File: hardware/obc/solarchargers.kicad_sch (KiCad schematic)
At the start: 36 parts, among them U105 LTC4121, U402 LTC4121

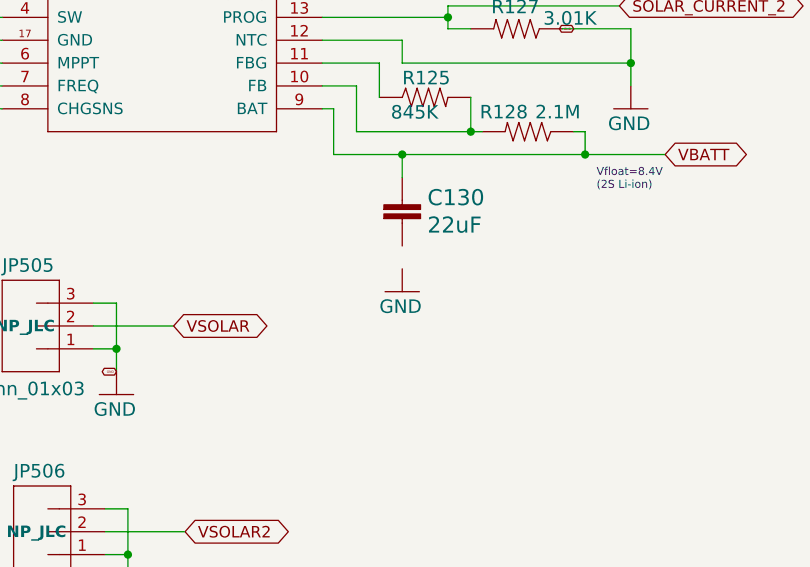
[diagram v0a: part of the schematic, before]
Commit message: OBC: Continuing work towards the next revision
- tidied up Radio and GPS page
- moved J305 to Avionics page
- changed R423 to 1.5k
- removed R428 so ILIM pin connects directly to GNDREF
- changed L403 to 4.7uH
- deleted BOM fields proto and flight
- connected C130 to ground
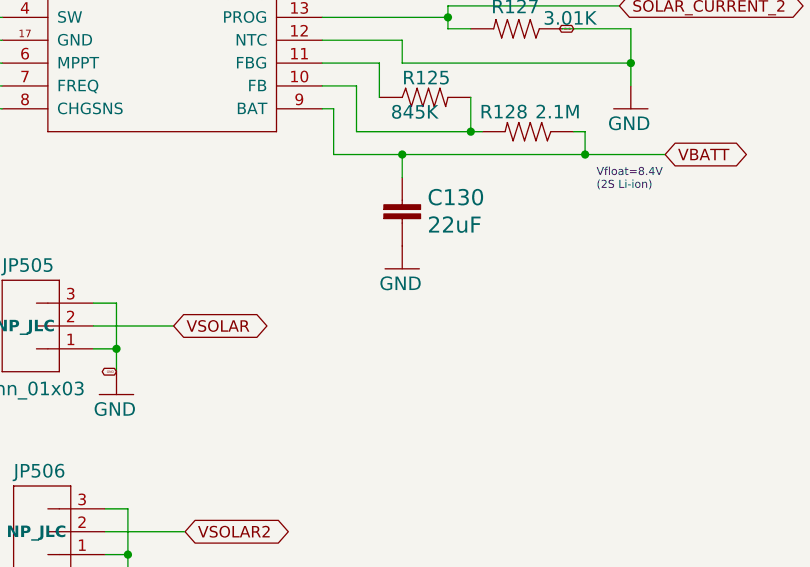
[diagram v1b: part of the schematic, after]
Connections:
- net GND: now also C130.2
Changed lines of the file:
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@@
 	(symbol
 		(lib_id "mainboard:GND")
-		(at 146.05 153.67 0)
+		(at 146.05 151.13 0)
 		(unit 1)
 		(exclude_from_sim no)
@@
 		(dnp no)
 		(property "Reference" "#GND0124"
-			(at 146.05 153.67 0)
+			(at 146.05 151.13 0)
 			(effects
 				(font
@@
 		)
 		(property "Value" "GND"
-			(at 143.51 156.21 0)
+			(at 143.51 153.67 0)
 			(effects
 				(font
@@
 		)
 		(property "Footprint" ""
-			(at 146.05 153.67 0)
+			(at 146.05 151.13 0)
 			(effects
 				(font
@@
 		)
 		(property "Datasheet" ""
-			(at 146.05 153.67 0)
+			(at 146.05 151.13 0)
 			(effects
 				(font
@@
 		)
 		(property "Description" ""
-			(at 146.05 153.67 0)
+			(at 146.05 151.13 0)
 			(effects
 				(font

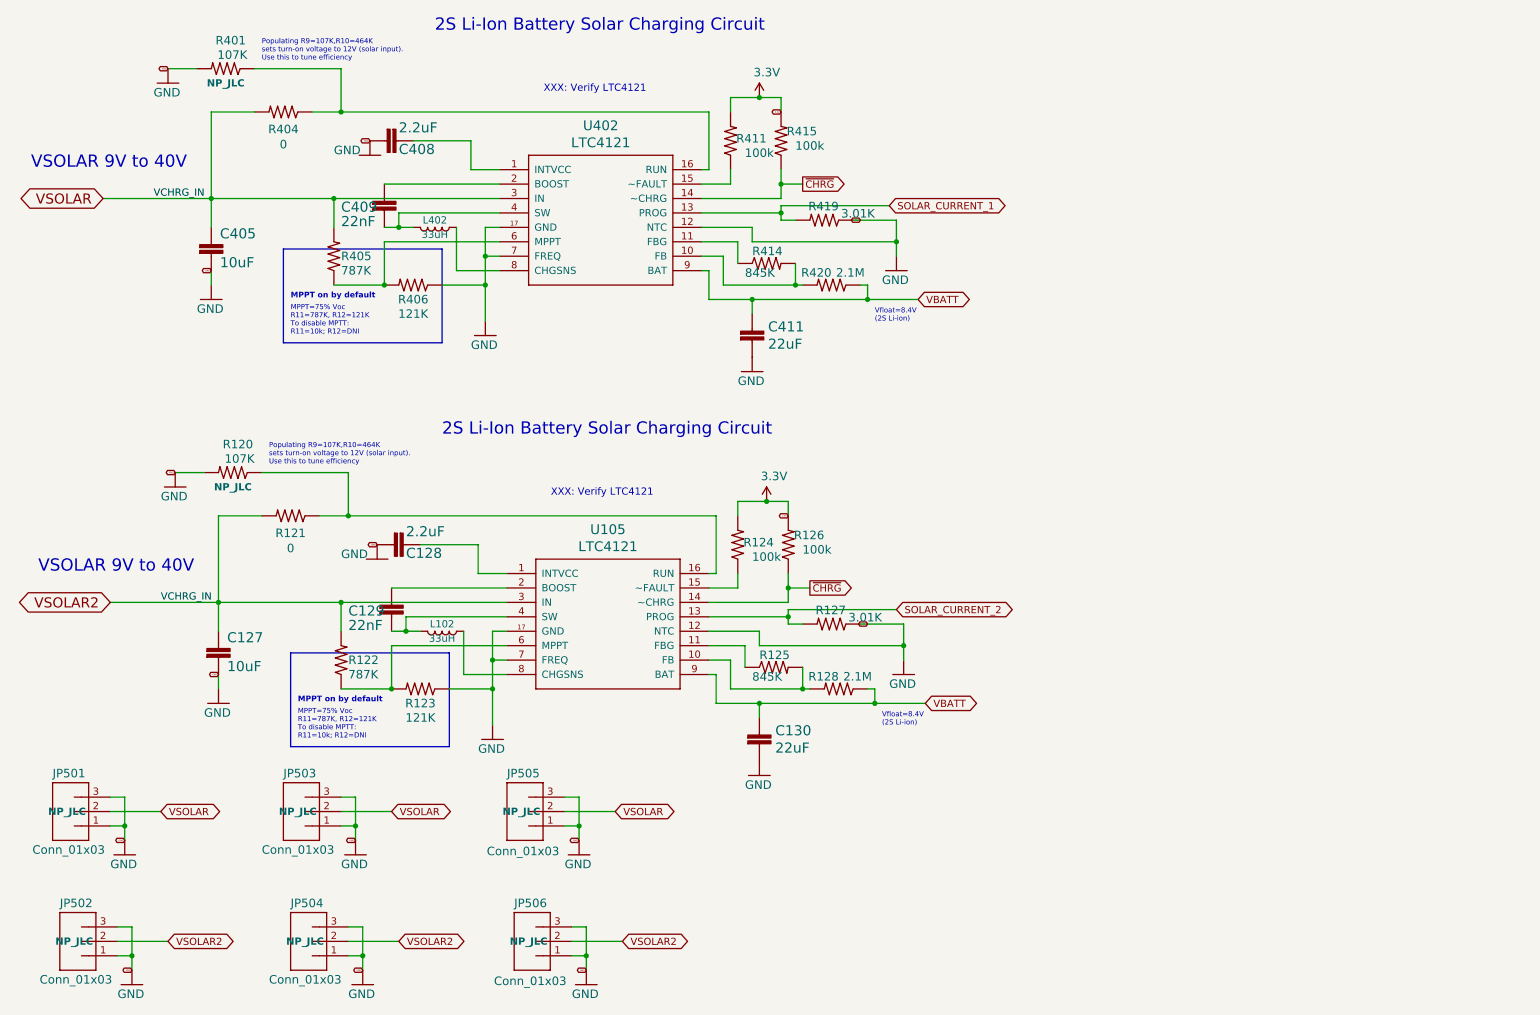
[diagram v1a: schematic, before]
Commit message: OBC: Continuing work towards the next revision
- moved Jtag to Avionics page
- re-aligned and removed excess text
- flipped watchdog to make +3.3v face up
- cleaned up VREG pins, crystal, SWCLK, SWDIO, and watch dog connections
- fixed MRAM symbol
- changed USB_D +/- resistor values
- spaced out schematics on power and burn wire pages
- fixed GNDREF connection for J302
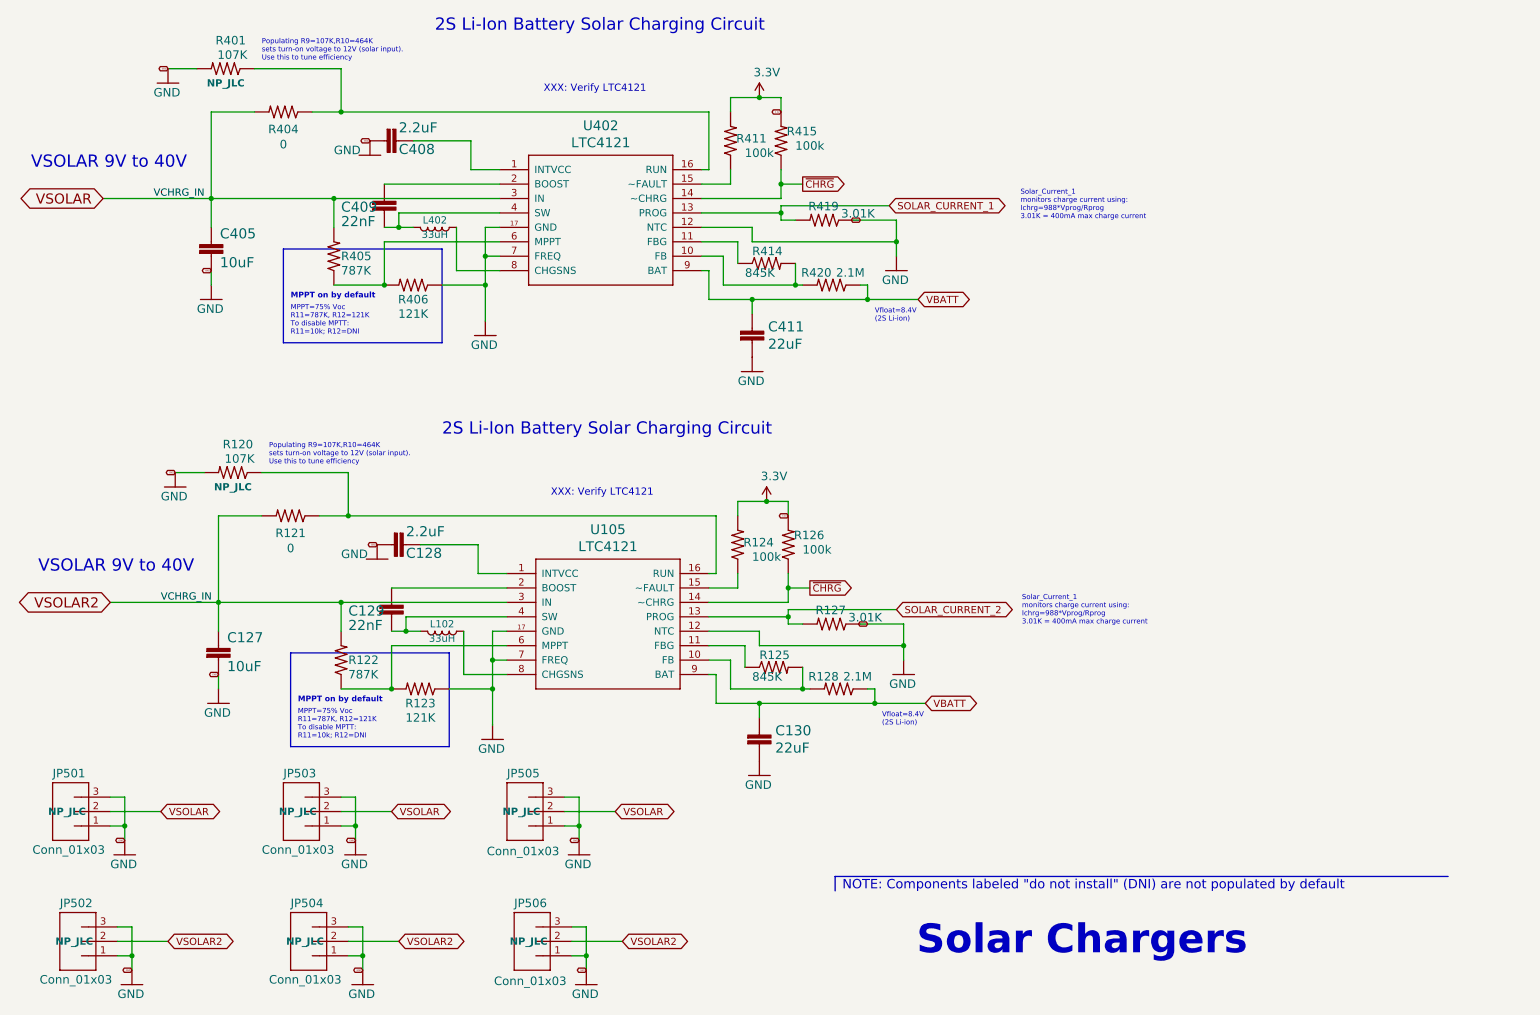
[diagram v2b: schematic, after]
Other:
- note added: "NOTE: Components labeled "do not install" (DNI) are not populated by default"
- note added: "Solar Chargers"
- note added: "Solar_Current_1 monitors charge current using: Ichrg=988*Vprog/Rprog 3.01K = 400mA max charge current"
- title: (none) -> Obi Wan Computer
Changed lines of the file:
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@@
 	(generator "eeschema")
 	(generator_version "8.0")
-	(paper "A4")
+	(paper "USLetter")
+	(title_block
+		(title "Obi Wan Computer")
+		(rev "1")
+	)
 	(junction
 		(at 166.37 138.43)
@@
 		)
 	)
+	(polyline
+		(pts
+			(xy 159.385 171.45) (xy 159.385 168.91)
+		)
+		(stroke
+			(width 0)
+			(type default)
+		)
+	)
 	(wire
 		(pts
@@
 		(pts
 			(xy 49.53 34.29) (xy 49.53 49.53)
+		)
+		(stroke
+			(width 0)
+			(type default)
+		)
+	)
+	(polyline
+		(pts
+			(xy 159.385 168.91) (xy 267.335 168.91)
 		)
 		(stroke
@@
 			(font
 				(size 0.889 0.889)
+			)
+			(justify left bottom)
+		)
+	)
+	(text "NOTE: Components labeled \"do not install\" (DNI) are not populated by default"
+		(exclude_from_sim no)
+		(at 160.655 171.45 0)
+		(effects
+			(font
+				(size 1.651 1.651)
 			)
 			(justify left bottom)
@@
 		)
 	)
+	(text "Solar Chargers"
+		(exclude_from_sim no)
+		(at 173.736 183.134 0)
+		(effects
+			(font
+				(size 5.08 5.08)
+				(thickness 1.016)
+				(bold yes)
+			)
+			(justify left bottom)
+		)
+	)
 	(text "\nMPPT=75% Voc\nR11=787K, R12=121K\nTo disable MPTT:\nR11=10k; R12=DNI"
 		(exclude_from_sim no)
@@
 			)
 			(justify left bottom)
+		)
+	)
+	(text "Solar_Current_1\nmonitors charge current using:\nIchrg=988*Vprog/Rprog\n3.01K = 400mA max charge current\n"
+		(exclude_from_sim no)
+		(at 192.278 124.714 0)
+		(effects
+			(font
+				(size 0.889 0.889)
+			)
+			(justify left bottom)
+		)
+	)
+	(text "Solar_Current_1\nmonitors charge current using:\nIchrg=988*Vprog/Rprog\n3.01K = 400mA max charge current\n"
+		(exclude_from_sim no)
+		(at 192.024 53.34 0)
+		(effects
+			(font
+				(size 0.889 0.889)
+			)
+			(justify left bottom)

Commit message: OBC: Continuing work towards the next revision
- Cleaned up text on Avionics Page
- Changed some descriptions and cleaned up text on Power Page
- Changed Power Relay A schematic to one from PCB
- Changed R120 and R401 changed from 107k to 34.8k and changed R121 and R404 from 0 to 10k and R127 and R419 from 3.01k to 3.83k (Solar Chargers Page)
- Checked R303 and R304 resistor value and believe 27 is correct
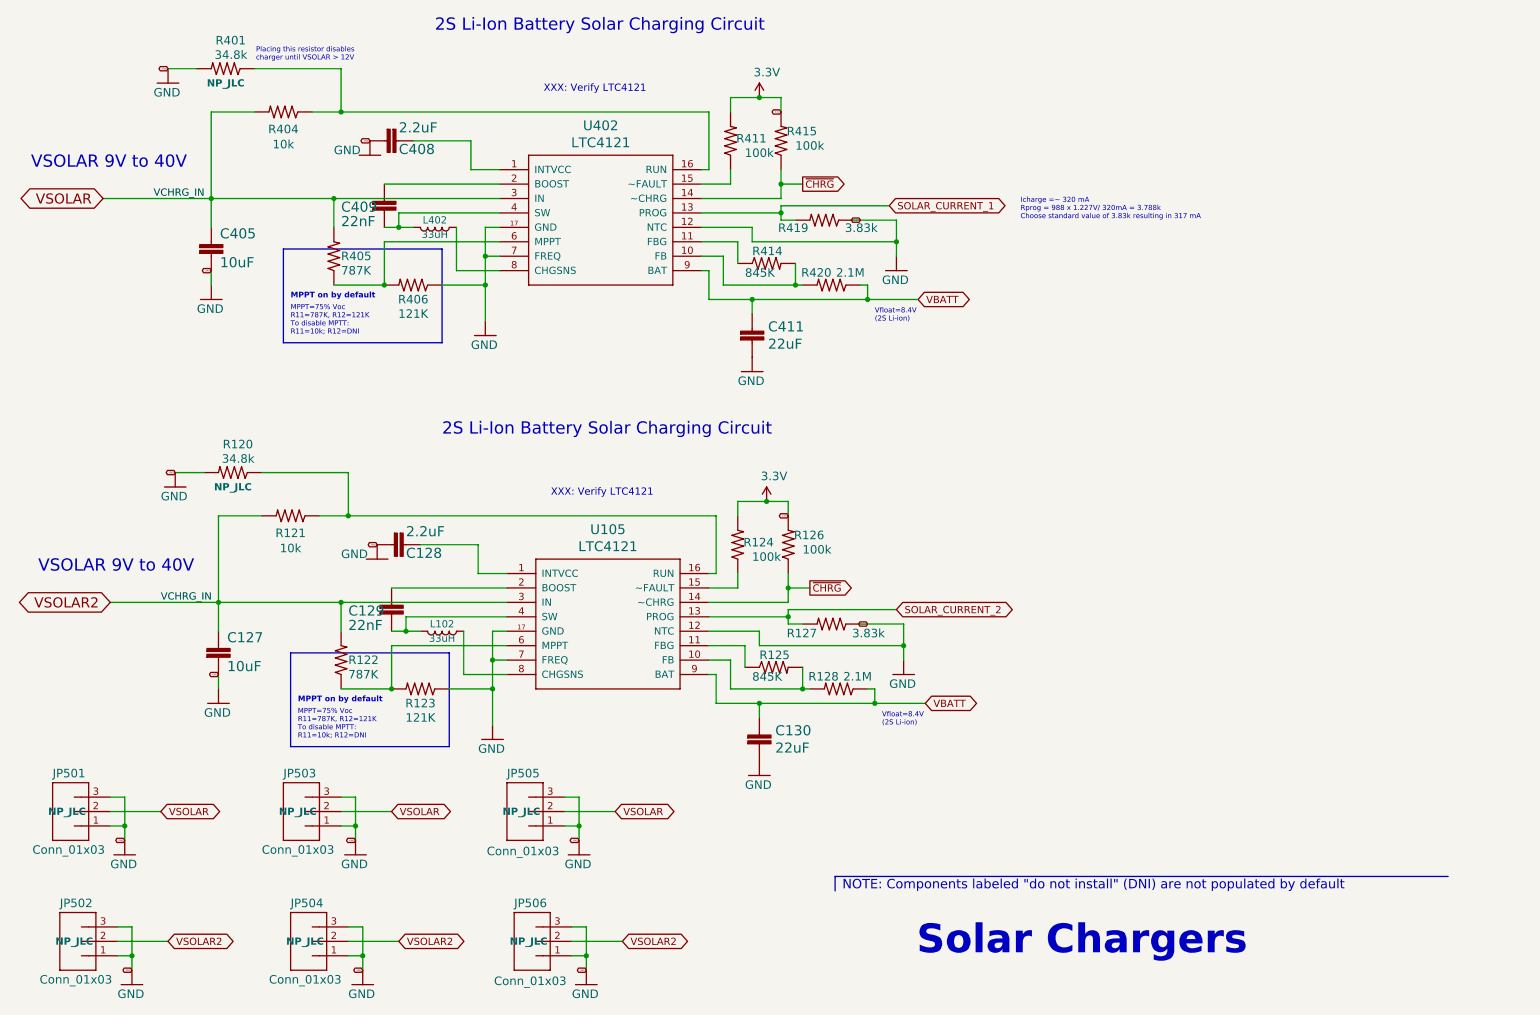
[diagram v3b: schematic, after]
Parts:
- R120, R401: value 107K -> 34.8k
- R121, R404: value 0 -> 10k; LCSC C2654002 -> (none); Manufacturer_Name Vishay Intertech -> (none); Manufacturer_Part_Number MCT06030Z0000ZP500 -> (none)
- R127, R419: value 3.01K -> 3.83k; LCSC C137732 -> (none)
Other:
- note added: "Icharge =~ 320 mA Rprog = 988 x 1.227V/ 320mA = 3.788k Choose standard value of 3.83k resulting in 317 mA"
- note added: "Placing this resistor disables charger until VSOLAR > 12V"
- note removed: "Populating R9=107K,R10=464K sets turn-on voltage to 12V (solar input). Use this to tune efficiency"
- note removed: "Solar_Current_1 monitors charge current using: Ichrg=988*Vprog/Rprog 3.01K = 400mA max charge current"
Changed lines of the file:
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@@
 		)
 	)
-	(text "Populating R9=107K,R10=464K\nsets turn-on voltage to 12V (solar input). \nUse this to tune efficiency"
+	(text "Placing this resistor disables \ncharger until VSOLAR > 12V"
 		(exclude_from_sim no)
-		(at 58.42 25.4 0)
-		(effects
-			(font
-				(size 0.889 0.889)
-			)
-			(justify left bottom)
-		)
-	)
-	(text "Populating R9=107K,R10=464K\nsets turn-on voltage to 12V (solar input). \nUse this to tune efficiency"
-		(exclude_from_sim no)
-		(at 59.69 96.52 0)
+		(at 57.404 25.4 0)
 		(effects
 			(font
@@
 		)
 	)
-	(text "Solar_Current_1\nmonitors charge current using:\nIchrg=988*Vprog/Rprog\n3.01K = 400mA max charge current\n"
-		(exclude_from_sim no)
-		(at 192.278 124.714 0)
-		(effects
-			(font
-				(size 0.889 0.889)
-			)
-			(justify left bottom)
-		)
-	)
-	(text "Solar_Current_1\nmonitors charge current using:\nIchrg=988*Vprog/Rprog\n3.01K = 400mA max charge current\n"
+	(text "Icharge =~ 320 mA\nRprog = 988 x 1.227V/ 320mA = 3.788k\nChoose standard value of 3.83k resulting in 317 mA"
 		(exclude_from_sim no)
 		(at 192.024 53.34 0)
@@
 			)
 		)
-		(property "Value" "107K"
+		(property "Value" "34.8k"
 			(at 57.15 94.488 0)
 			(effects
@@
 			)
 		)
-		(property "Description" "107K 0603"
+		(property "Description" ""
 			(at 54.61 95.25 0)
 			(effects
@@
 		(dnp no)
 		(property "Reference" "R419"
-			(at 160.02 50.038 0)
+			(at 154.686 53.848 0)
 			(effects
 				(font
@@
 			)
 		)
-		(property "Value" "3.01K"
-			(at 166.37 51.308 0)
+		(property "Value" "3.83k"
+			(at 166.878 53.848 0)
 			(effects
 				(font
@@
 			)
 		)
-		(property "Description" "3.01K 0603"
+		(property "Description" ""
 			(at 156.21 52.2986 0)
 			(effects
@@
 			)
 		)
-		(property "LCSC" "C137732"
+		(property "LCSC" ""
 			(at 157.48 53.34 0)
 			(effects
@@
 			)
 		)
-		(property "Value" "0"
+		(property "Value" "10k"
 			(at 62.23 40.005 0)
 			(effects
@@
 			)
 		)
-		(property "LCSC" "C2654002"
+		(property "LCSC" ""
 			(at 62.23 34.29 0)
 			(effects
@@
 			)
 		)
-		(property "Manufacturer_Name" " Vishay Intertech"
+		(property "Manufacturer_Name" ""
 			(at 62.23 34.29 0)
 			(effects
@@
 			)
 		)
-		(property "Manufacturer_Part_Number" " MCT06030Z0000ZP500"
+		(property "Manufacturer_Part_Number" ""
 			(at 62.23 34.29 0)
 			(effects
@@
 		(dnp no)
 		(property "Reference" "R127"
-			(at 161.29 121.158 0)
+			(at 156.21 125.222 0)
 			(effects
 				(font
@@
 			)
 		)
-		(property "Value" "3.01K"
-			(at 167.64 122.428 0)
+		(property "Value" "3.83k"
+			(at 168.148 125.222 0)
 			(effects
 				(font
@@
 			)
 		)
-		(property "Description" "3.01K 0603"
+		(property "Description" ""
 			(at 157.48 123.4186 0)
 			(effects
@@
 			)
 		)
-		(property "LCSC" "C137732"
+		(property "LCSC" ""
 			(at 158.75 124.46 0)
 			(effects
@@
 			)
 		)
-		(property "Value" "0"
+		(property "Value" "10k"
 			(at 63.5 111.125 0)
 			(effects
@@
 			)
 		)
-		(property "LCSC" "C2654002"
+		(property "LCSC" ""
 			(at 63.5 105.41 0)
 			(effects
@@
 			)
 		)
-		(property "Manufacturer_Name" " Vishay Intertech"
+		(property "Manufacturer_Name" ""
 			(at 63.5 105.41 0)
 			(effects
@@
 			)
 		)
-		(property "Manufacturer_Part_Number" " MCT06030Z0000ZP500"
+		(property "Manufacturer_Part_Number" ""
 			(at 63.5 105.41 0)
 			(effects
@@
 			)
 		)
-		(property "Value" "107K"
+		(property "Value" "34.8k"
 			(at 55.88 23.368 0)
 			(effects
@@
 			)
 		)
-		(property "Description" "107K 0603"
+		(property "Description" ""
 			(at 53.34 24.13 0)
 			(effects

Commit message: obc: Fixed errors from design review
- Gave proper attribution on all pages
- Spread out components on Avionics page
- Changed GPS power circuit
- Added a DNP resistor in between VBATT and VWATCHEDRAIL
- Added various other part numbers on Power Supervisor and Watch Dog Page
- Changed Power Supervisor and Watch Dog Page to page 3
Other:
- company: (none) -> Luke Titi, Michael Lyle
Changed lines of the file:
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@@
 		(title "Obi Wan Computer")
 		(rev "1")
+		(company "Luke Titi, Michael Lyle")
 	)
 	(junction

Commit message: obc: Fixed second design review, and fixed up BOM
- added layout comments on schematic
- fixed various comments
- added many LCSC # for components
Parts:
- R121, R404: LCSC (none) -> C169849
- R127, R419: LCSC (none) -> C482840
